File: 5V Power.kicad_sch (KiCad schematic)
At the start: 18 parts, among them U3 TPS54540BDDA

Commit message: updates to BOM and power connections
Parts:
- C_1, C_2, C_3, C_4: value 4.7u -> 4.7uF
- C_5: value 100n -> 0.1u; Digikey (none) -> 1276-1003-1-ND; LCSC (none) -> C1711; MPN (none) -> CL21B104KBCNNNC; Manufacturer (none) -> Samsung Electro-Mechanics
- L_1: value 4.7u -> 4.7uH
- U3: footprint (none) -> LEOS:SO-POWERPAD8_DDA_TEX; Digikey (none) -> 296-TPS54540BDDA-ND; MPN (none) -> TPS54540BDDA; Manufacturer (none) -> Texas Instruments
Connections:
- net VIN renamed VPP
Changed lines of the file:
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@@
-		)
-	)
-	(hierarchical_label "VIN"
-		(shape input)
-		(at 38.1 90.17 180)
-		(effects
-			(font
-				(size 1.27 1.27)
-			)
-			(justify right)
 		)
 	)
@@
 			)
 		)
-		(property "Value" "4.7u"
+		(property "Value" "4.7uF"
 			(at 57.658 97.282 0)
 			(show_name no)
@@
 	)
 	(symbol
+		(lib_id "power:VPP")
+		(at 38.1 90.17 0)
+		(unit 1)
+		(body_style 1)
+		(exclude_from_sim no)
+		(in_bom yes)
+		(on_board yes)
+		(in_pos_files yes)
+		(dnp no)
+		(fields_autoplaced yes)
+		(property "Reference" "#PWR046"
+			(at 38.1 93.98 0)
+			(hide yes)
+			(show_name no)
+			(do_not_autoplace no)
+			(effects
+				(font
+					(size 1.27 1.27)
+				)
+			)
+		)
+		(property "Value" "VPP"
+			(at 38.1 85.09 0)
+			(show_name no)
+			(do_not_autoplace no)
+			(effects
+				(font
+					(size 1.27 1.27)
+				)
+			)
+		)
+		(property "Footprint" ""
+			(at 38.1 90.17 0)
+			(hide yes)
+			(show_name no)
+			(do_not_autoplace no)
+			(effects
+				(font
+					(size 1.27 1.27)
+				)
+			)
+		)
+		(property "Datasheet" ""
+			(at 38.1 90.17 0)
+			(hide yes)
+			(show_name no)
+			(do_not_autoplace no)
+			(effects
+				(font
+					(size 1.27 1.27)
+				)
+			)
+		)
+		(property "Description" "Power symbol creates a global label with name \"VPP\""
+			(at 38.1 90.17 0)
+			(hide yes)
+			(show_name no)
+			(do_not_autoplace no)
+			(effects
+				(font
+					(size 1.27 1.27)
+				)
+			)
+		)
+		(pin "1"
+		)
+		(instances
+			(project "LEOS-F26-power"
+				(path "/3703ddf2-8141-438d-86a8-1eaec9672d0d/528ff9b0-a904-4a78-86c6-11cbf84face6"
+					(reference "#PWR046")
+					(unit 1)
+				)
+			)
+		)
+	)
+	(symbol
 		(lib_id "Device:C")
 		(at 46.99 95.25 0)
@@
 			)
 		)
-		(property "Value" "4.7u"
+		(property "Value" "4.7uF"
 			(at 41.402 97.282 0)
 			(show_name no)
@@
 			)
 		)
-		(property "Footprint" ""
+		(property "Footprint" "LEOS:SO-POWERPAD8_DDA_TEX"
 			(at 99.06 87.63 0)
 			(hide yes)
@@
 		)
 		(property "Description" ""
+			(at 99.06 87.63 0)
+			(hide yes)
+			(show_name no)
+			(do_not_autoplace no)
+			(effects
+				(font
+					(size 1.27 1.27)
+				)
+			)
+		)
+		(property "Digikey" "296-TPS54540BDDA-ND"
+			(at 99.06 87.63 0)
+			(hide yes)
+			(show_name no)
+			(do_not_autoplace no)
+			(effects
+				(font
+					(size 1.27 1.27)
+				)
+			)
+		)
+		(property "MPN" "TPS54540BDDA"
+			(at 99.06 87.63 0)
+			(hide yes)
+			(show_name no)
+			(do_not_autoplace no)
+			(effects
+				(font
+					(size 1.27 1.27)
+				)
+			)
+		)
+		(property "Manufacturer" "Texas Instruments"
 			(at 99.06 87.63 0)
 			(hide yes)
@@
 			)
 		)
-		(property "Value" "4.7u"
+		(property "Value" "4.7uH"
 			(at 171.45 69.85 90)
 			(show_name no)
@@
 			)
 		)
-		(property "Value" "4.7u"
+		(property "Value" "4.7uF"
 			(at 50.038 97.536 0)
 			(show_name no)
@@
 			)
 		)
-		(property "Value" "4.7u"
+		(property "Value" "4.7uF"
 			(at 65.024 97.536 0)
 			(show_name no)
@@
 			)
 		)
-		(property "Value" "100n"
+		(property "Value" "0.1u"
 			(at 120.65 67.31 90)
 			(show_name no)
@@
 			)
 		)
-		(property "Description" "Unpolarized capacitor"
+		(property "Description" "0.1uF 50V X7R 0805"
 			(at 120.65 72.39 0)
 			(hide yes)
 			(show_name no)
+			(do_not_autoplace no)
+			(effects
+				(font
+					(size 1.27 1.27)
+				)
+			)
+		)
+		(property "Digikey" "1276-1003-1-ND"
+			(at 120.65 72.39 90)
+			(hide yes)
+			(show_name no)
+			(do_not_autoplace no)
+			(effects
+				(font
+					(size 1.27 1.27)
+				)
+			)
+		)
+		(property "LCSC" "C1711"
+			(at 120.65 72.39 90)
+			(hide yes)
+			(show_name no)
+			(do_not_autoplace no)
+			(effects
+				(font
+					(size 1.27 1.27)
+				)
+			)
+		)
+		(property "MPN" "CL21B104KBCNNNC"
+			(at 120.65 72.39 90)
+			(hide yes)
+			(show_name no)
+			(do_not_autoplace no)
+			(effects
+				(font
+					(size 1.27 1.27)
+				)
+			)
+		)
+		(property "Manufacturer" "Samsung Electro-Mechanics"
+			(at 120.65 72.39 90)
+			(hide yes)
+			(show_name no)

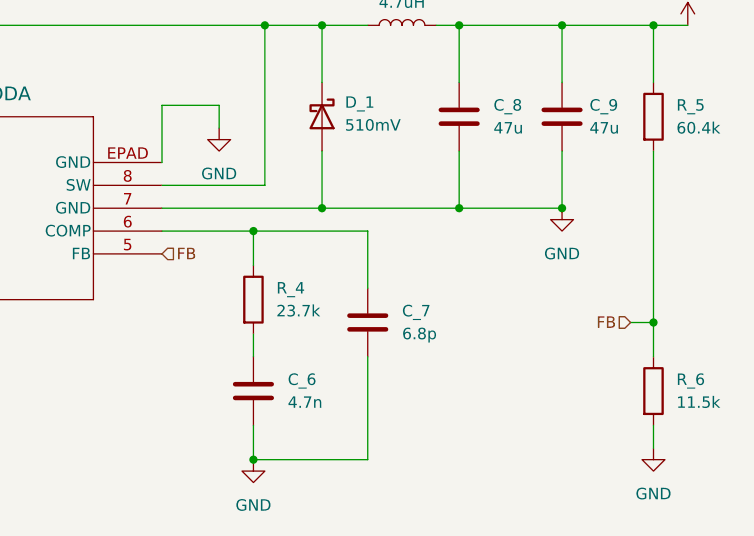
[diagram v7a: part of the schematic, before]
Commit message: updates to BOM and fixes for ERC
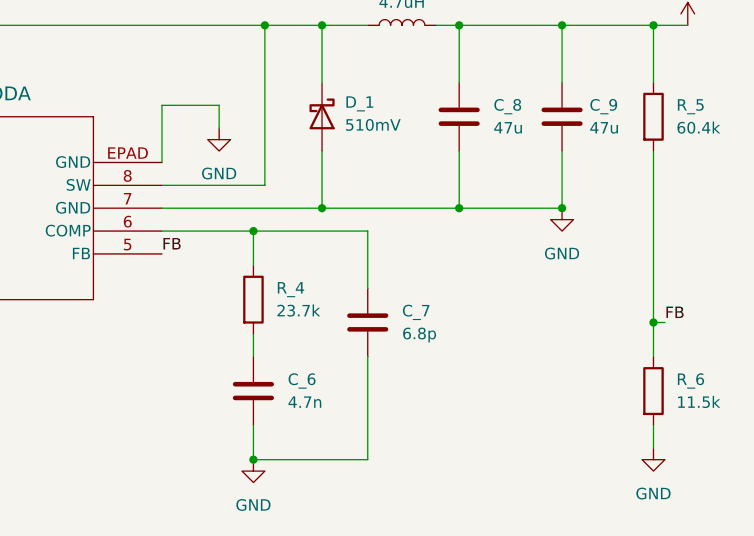
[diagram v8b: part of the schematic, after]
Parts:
- C_8, C_9: footprint Capacitor_SMD:C_0805_2012Metric -> Capacitor_SMD:C_1206_3216Metric; Digikey (none) -> 4713-GMC31X5R476M25NTCT-ND; MPN (none) -> GMC31X5R476M25NT; Manufacturer (none) -> Cal-Chip Electronics, Inc.
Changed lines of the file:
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@@
+	)
+	(junction
+		(at 199.39 105.41)
+		(diameter 0)
+		(color 0 0 0 0)
 	)
 	(junction
@@
 	)
 	(junction
-		(at 199.39 105.41)
-		(diameter 0)
-		(color 0 0 0 0)
-	)
-	(junction
 		(at 189.23 92.71)
 		(diameter 0)
@@
 	(wire
 		(pts
-			(xy 196.85 105.41) (xy 199.39 105.41)
-		)
-		(stroke
-			(width 0)
-			(type default)
-		)
-	)
-	(wire
-		(pts
 			(xy 144.78 81.28) (xy 151.13 81.28)
 		)
@@
 	(wire
 		(pts
+			(xy 199.39 105.41) (xy 200.66 105.41)
+		)
+		(stroke
+			(width 0)
+			(type default)
+		)
+	)
+	(wire
+		(pts
 			(xy 99.06 92.71) (xy 88.9 92.71)
 		)
@@
 	(wire
 		(pts
+			(xy 162.56 72.39) (xy 167.64 72.39)
+		)
+		(stroke
+			(width 0)
+			(type default)
+		)
+	)
+	(wire
+		(pts
+			(xy 199.39 119.38) (xy 199.39 116.84)
+		)
+		(stroke
+			(width 0)
+			(type default)
+		)
+	)
+	(wire
+		(pts
+			(xy 69.85 101.6) (xy 62.23 101.6)
+		)
+		(stroke
+			(width 0)
+			(type default)
+		)
+	)
+	(wire
+		(pts
+			(xy 144.78 90.17) (xy 156.21 90.17)
+		)
+		(stroke
+			(width 0)
+			(type default)
+		)
+	)
+	(wire
+		(pts
+			(xy 177.8 72.39) (xy 177.8 78.74)
+		)
+		(stroke
+			(width 0)
+			(type default)
+		)
+	)
+	(wire
+		(pts
+			(xy 82.55 114.3) (xy 92.71 114.3)
+		)
+		(stroke
+			(width 0)
+			(type default)
+		)
+	)
+	(wire
+		(pts
+			(xy 99.06 95.25) (xy 92.71 95.25)
+		)
+		(stroke
+			(width 0)
+			(type default)
+		)
+	)
+	(wire
+		(pts
+			(xy 69.85 90.17) (xy 82.55 90.17)
+		)
+		(stroke
+			(width 0)
+			(type default)
+		)
+	)
+	(wire
+		(pts
+			(xy 144.78 92.71) (xy 162.56 92.71)
+		)
+		(stroke
+			(width 0)
+			(type default)
+		)
+	)
+	(wire
+		(pts
 			(xy 199.39 105.41) (xy 199.39 109.22)
 		)
@@
 	(wire
 		(pts
-			(xy 162.56 72.39) (xy 167.64 72.39)
-		)
-		(stroke
-			(width 0)
-			(type default)
-		)
-	)
-	(wire
-		(pts
-			(xy 199.39 119.38) (xy 199.39 116.84)
-		)
-		(stroke
-			(width 0)
-			(type default)
-		)
-	)
-	(wire
-		(pts
-			(xy 69.85 101.6) (xy 62.23 101.6)
-		)
-		(stroke
-			(width 0)
-			(type default)
-		)
-	)
-	(wire
-		(pts
-			(xy 144.78 90.17) (xy 156.21 90.17)
-		)
-		(stroke
-			(width 0)
-			(type default)
-		)
-	)
-	(wire
-		(pts
-			(xy 177.8 72.39) (xy 177.8 78.74)
-		)
-		(stroke
-			(width 0)
-			(type default)
-		)
-	)
-	(wire
-		(pts
-			(xy 82.55 114.3) (xy 92.71 114.3)
-		)
-		(stroke
-			(width 0)
-			(type default)
-		)
-	)
-	(wire
-		(pts
-			(xy 99.06 95.25) (xy 92.71 95.25)
-		)
-		(stroke
-			(width 0)
-			(type default)
-		)
-	)
-	(wire
-		(pts
-			(xy 69.85 90.17) (xy 82.55 90.17)
-		)
-		(stroke
-			(width 0)
-			(type default)
-		)
-	)
-	(wire
-		(pts
-			(xy 144.78 92.71) (xy 162.56 92.71)
-		)
-		(stroke
-			(width 0)
-			(type default)
-		)
-	)
-	(wire
-		(pts
 			(xy 62.23 90.17) (xy 69.85 90.17)
 		)
@@
 		)
 	)
-	(hierarchical_label "FB"
-		(shape input)
-		(at 196.85 105.41 180)
-		(effects
-			(font
-				(size 1.27 1.27)
-			)
-			(justify right)
-		)
-	)
-	(hierarchical_label "FB"
-		(shape input)
+	(label "FB"
 		(at 144.78 97.79 0)
 		(effects
@@
 				(size 1.27 1.27)
 			)
-			(justify left)
+			(justify left bottom)
+		)
+	)
+	(label "FB"
+		(at 200.66 105.41 0)
+		(effects
+			(font
+				(size 1.27 1.27)
+			)
+			(justify left bottom)
 		)
 	)
@@
 			)
 		)
-		(property "Footprint" "Capacitor_SMD:C_0805_2012Metric"
+		(property "Footprint" "Capacitor_SMD:C_1206_3216Metric"
 			(at 178.7652 86.36 0)
 			(hide yes)
@@
 		)
 		(property "Description" "Unpolarized capacitor"
+			(at 177.8 82.55 0)
+			(hide yes)
+			(show_name no)
+			(do_not_autoplace no)
+			(effects
+				(font
+					(size 1.27 1.27)
+				)
+			)
+		)
+		(property "Digikey" "4713-GMC31X5R476M25NTCT-ND"
+			(at 177.8 82.55 0)
+			(hide yes)
+			(show_name no)
+			(do_not_autoplace no)
+			(effects
+				(font
+					(size 1.27 1.27)
+				)
+			)
+		)
+		(property "MPN" "GMC31X5R476M25NT"
+			(at 177.8 82.55 0)
+			(hide yes)
+			(show_name no)
+			(do_not_autoplace no)
+			(effects
+				(font
+					(size 1.27 1.27)
+				)
+			)
+		)
+		(property "Manufacturer" "Cal-Chip Electronics, Inc."
 			(at 177.8 82.55 0)
 			(hide yes)
@@
 			)
 		)
-		(property "Footprint" "Capacitor_SMD:C_0805_2012Metric"
+		(property "Footprint" "Capacitor_SMD:C_1206_3216Metric"
 			(at 190.1952 86.36 0)
 			(hide yes)
@@
 			(at 189.23 82.55 0)
 			(hide yes)
+			(show_name no)
+			(do_not_autoplace no)
+			(effects
+				(font
+					(size 1.27 1.27)
+				)
+			)
+		)
+		(property "Digikey" "4713-GMC31X5R476M25NTCT-ND"
+			(at 189.23 82.55 0)
+			(hide yes)
+			(show_name no)
+			(do_not_autoplace no)
+			(effects
+				(font
+					(size 1.27 1.27)
+				)
+			)
+		)
+		(property "MPN" "GMC31X5R476M25NT"
+			(at 189.23 82.55 0)
+			(hide yes)
+			(show_name no)
+			(do_not_autoplace no)
+			(effects
+				(font
+					(size 1.27 1.27)
+				)
+			)
+		)
+		(property "Manufacturer" "Cal-Chip Electronics, Inc."
+			(at 189.23 82.55 0)
+			(hide yes)
